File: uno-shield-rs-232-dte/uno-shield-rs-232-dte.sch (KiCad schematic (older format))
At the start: 19 parts, among them J1 Ctrl Route, J3 DSR/CTS, J4 DB9_Male, P1 Power, P2 Analog, P3 Digital, P4 Digital, P5 CONN_01X01, P7 CONN_01X01, U1 MAX232

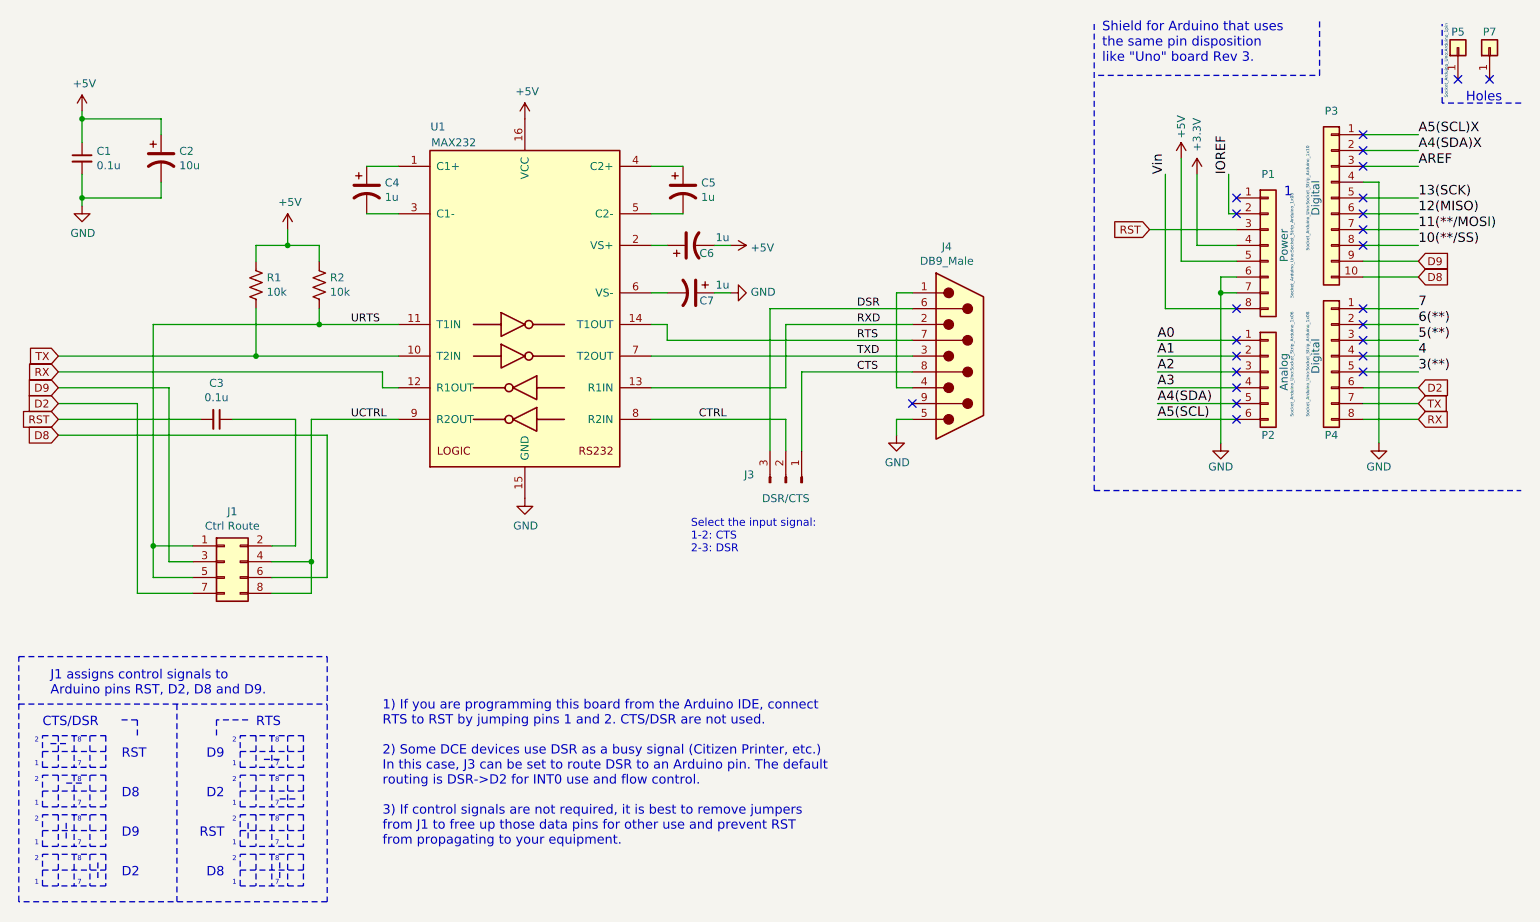
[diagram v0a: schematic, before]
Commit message: Adjust DTE shield to allow UART routing.
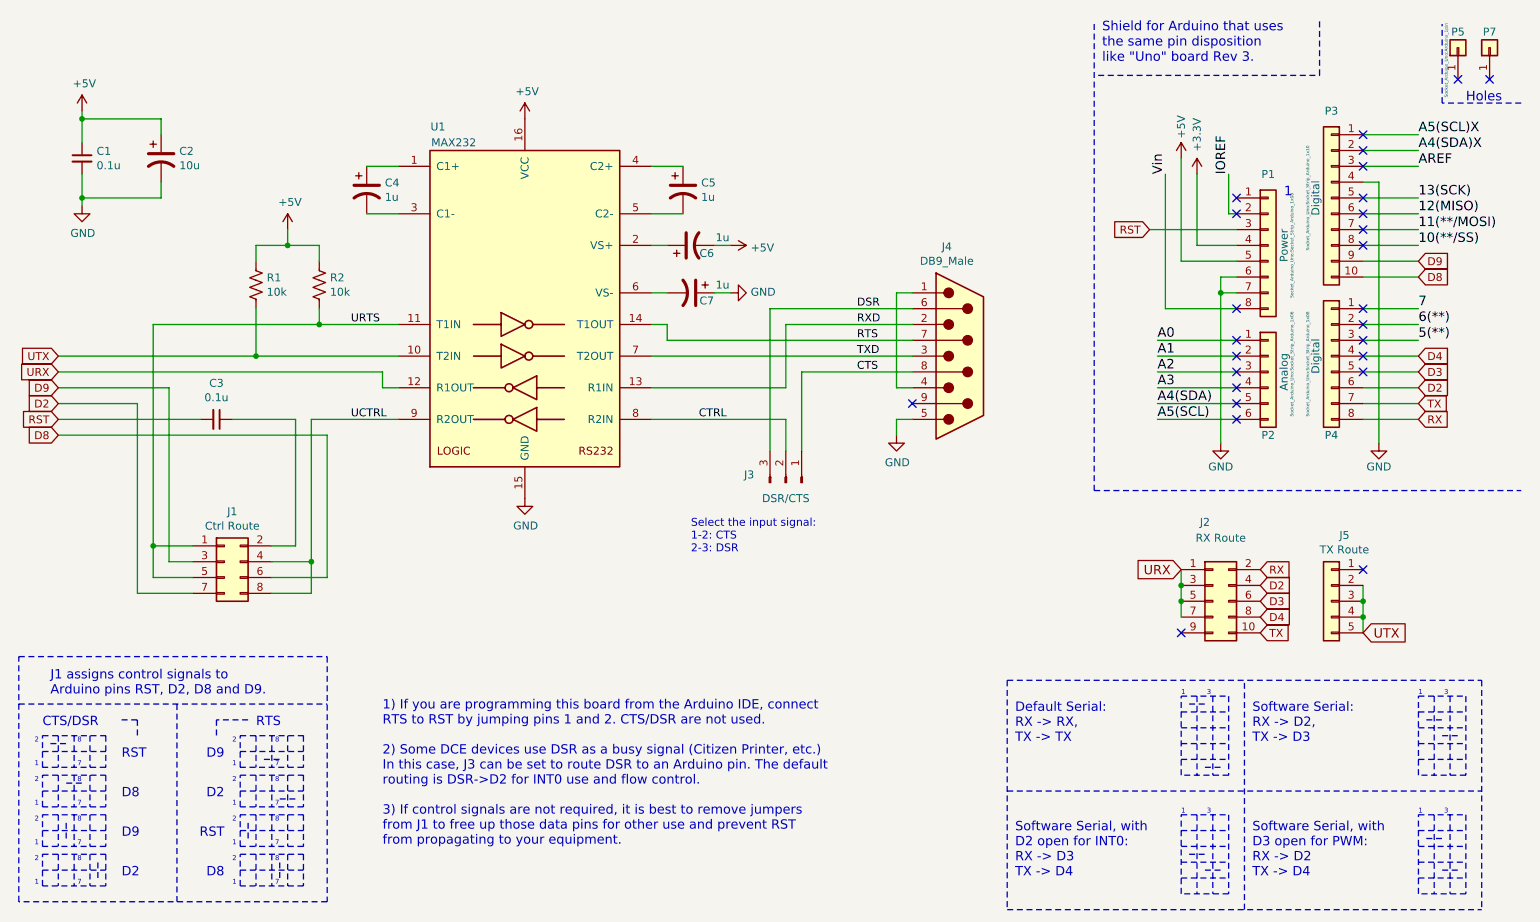
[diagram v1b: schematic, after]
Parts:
- added J2: RX Route, Connector_PinHeader_2.54mm:PinHeader_2x05_P2.54mm_Vertical, symbol Connector_Generic:Conn_02x05_Odd_Even
- added J5: TX Route, Connector_PinHeader_2.54mm:PinHeader_1x05_P2.54mm_Vertical, symbol Connector_Generic:Conn_01x05
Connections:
- net D2: now also J2.4 (Pin_4)
- net RX: now also J2.2 (Pin_2); no longer U1.12 (R1OUT)
- net TX: now also J2.10 (Pin_10); no longer R1.2, U1.10 (T2IN)
- net 3(**) renamed D3
- net D3: now also J2.6 (Pin_6)
- net 4 renamed D4
- net D4: now also J2.8 (Pin_8)
- new net URX: J2.1 (Pin_1), J2.3 (Pin_3), J2.5 (Pin_5), J2.7 (Pin_7), U1.12 (R1OUT)
- new net UTX: J5.2 (Pin_2), J5.3 (Pin_3), J5.4 (Pin_4), J5.5 (Pin_5), R1.2, U1.10 (T2IN)
- no-connect marks 24 -> 26
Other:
- note added: "1 3"
- note added: "Default Serial:\nRX -> RX,\nTX -> TX"
- note added: "Software Serial, with\nD2 open for INT0:\nRX -> D3\nTX -> D4"
- note added: "Software Serial, with\nD3 open for PWM:\nRX -> D2\nTX -> D4"
- note added: "Software Serial:\nRX -> D2,\nTX -> D3"
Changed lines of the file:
@@
 Text Label 8150 3100 0    60   ~ 0
 A5(SCL)
-Text Label 9800 2800 0    60   ~ 0
-3(**)
-Text Label 9800 2700 0    60   ~ 0
-4
 Text Label 9800 2600 0    60   ~ 0
 5(**)
@@
 Connection ~ 1350 1700
 Text GLabel 1200 2700 0    50   Input ~ 0
-TX
+UTX
 Text GLabel 1200 2800 0    50   Input ~ 0
-RX
+URX
 Text GLabel 1200 2900 0    50   Input ~ 0
 D9
@@
 Text Notes 3250 5800 0    59   ~ 0
 1) If you are programming this board from the Arduino IDE, connect\nRTS to RST by jumping pins 1 and 2. CTS/DSR are not used.\n\n2) Some DCE devices use DSR as a busy signal (Citizen Printer, etc.)\nIn this case, J3 can be set to route DSR to an Arduino pin. The default\nrouting is DSR->D2 for INT0 use and flow control.\n\n3) If control signals are not required, it is best to remove jumpers\nfrom J1 to free up those data pins for other use and prevent RST\nfrom propagating to your equipment.
+Text GLabel 8800 4050 2    50   Input ~ 0
+RX
+Text GLabel 8800 4150 2    50   Input ~ 0
+D2
+Text GLabel 8800 4250 2    50   Input ~ 0
+D3
+Text GLabel 8800 4350 2    50   Input ~ 0
+D4
+Text GLabel 8300 4050 0    59   Input ~ 0
+URX
+Connection ~ 8300 4150
+Wire Wire Line
+	8300 4150 8300 4050
+Connection ~ 8300 4250
+Wire Wire Line
+	8300 4150 8300 4250
+Wire Wire Line
+	8300 4350 8300 4250
+$Comp
+L Connector_Generic:Conn_02x05_Odd_Even J2
+U 1 1 603B3853
+P 8500 4250
+F 0 "J2" H 8450 4750 50  0000 C CNN
+F 1 "RX Route" H 8550 4650 50  0000 C CNN
+F 2 "Connector_PinHeader_2.54mm:PinHeader_2x05_P2.54mm_Vertical" H 8500 4250 50  0001 C CNN
+F 3 "~" H 8500 4250 50  0001 C CNN
+	1    8500 4250
+	1    0    0    -1
+$EndComp
+Text GLabel 8800 4450 2    50   Input ~ 0
+TX
+$Comp
+L Connector_Generic:Conn_01x05 J5
+U 1 1 603DA995
+P 9250 4250
+F 0 "J5" H 9168 4667 50  0000 C CNN
+F 1 "TX Route" H 9168 4576 50  0000 C CNN
+F 2 "Connector_PinHeader_2.54mm:PinHeader_1x05_P2.54mm_Vertical" H 9250 4250 50  0001 C CNN
+F 3 "~" H 9250 4250 50  0001 C CNN
+	1    9250 4250
+	-1   0    0    -1
+$EndComp
+Wire Wire Line
+	9450 4150 9450 4250
+Wire Wire Line
+	9450 4250 9450 4350
+Connection ~ 9450 4250
+Wire Wire Line
+	9450 4350 9450 4450
+Connection ~ 9450 4350
+Text GLabel 9450 4450 2    59   Input ~ 0
+UTX
+NoConn ~ 9450 4050
+NoConn ~ 8300 4450
+Wire Notes Line
+	8300 4850 8600 4850
+Wire Notes Line
+	8600 4850 8600 5350
+Wire Notes Line
+	8600 5350 8300 5350
+Wire Notes Line
+	8300 5350 8300 4850
+Wire Notes Line
+	8300 4950 8600 4950
+Wire Notes Line
+	8300 5050 8600 5050
+Wire Notes Line
+	8300 5150 8600 5150
+Wire Notes Line
+	8300 5250 8600 5250
+Wire Notes Line
+	8400 4850 8400 5350
+Wire Notes Line
+	8500 4850 8500 5350
+Text Notes 8300 4850 0    31   ~ 0
+1          3
+Wire Notes Line
+	8300 5600 8600 5600
+Wire Notes Line
+	8600 5600 8600 6100
+Wire Notes Line
+	8600 6100 8300 6100
+Wire Notes Line
+	8300 6100 8300 5600
+Wire Notes Line
+	8300 5700 8600 5700
+Wire Notes Line
+	8300 5800 8600 5800
+Wire Notes Line
+	8300 5900 8600 5900
+Wire Notes Line
+	8300 6000 8600 6000
+Wire Notes Line
+	8400 5600 8400 6100
+Wire Notes Line
+	8500 5600 8500 6100
+Text Notes 8300 5600 0    31   ~ 0
+1          3
+Wire Notes Line
+	9800 4850 10100 4850
+Wire Notes Line
+	10100 4850 10100 5350
+Wire Notes Line
+	10100 5350 9800 5350
+Wire Notes Line
+	9800 5350 9800 4850
+Wire Notes Line
+	9800 4950 10100 4950
+Wire Notes Line
+	9800 5050 10100 5050
+Wire Notes Line
+	9800 5150 10100 5150
+Wire Notes Line
+	9800 5250 10100 5250
+Wire Notes Line
+	9900 4850 9900 5350
+Wire Notes Line
+	10000 4850 10000 5350
+Text Notes 9800 4850 0    31   ~ 0
+1          3
+Wire Notes Line
+	9800 5600 10100 5600
+Wire Notes Line
+	10100 5600 10100 6100
+Wire Notes Line
+	10100 6100 9800 6100
+Wire Notes Line
+	9800 6100 9800 5600
+Wire Notes Line
+	9800 5700 10100 5700
+Wire Notes Line
+	9800 5800 10100 5800
+Wire Notes Line
+	9800 5900 10100 5900
+Wire Notes Line
+	9800 6000 10100 6000
+Wire Notes Line
+	9900 5600 9900 6100
+Wire Notes Line
+	10000 5600 10000 6100
+Text Notes 9800 5600 0    31   ~ 0
+1          3
+Wire Notes Line width 100
+	8350 4900 8450 4900
+Wire Notes Line width 100
+	8450 5300 8550 5300
+Wire Notes Line width 100
+	9850 5000 9950 5000
+Wire Notes Line width 100
+	9950 5100 10050 5100
+Wire Notes Line width 100
+	9850 5750 9950 5750
+Wire Notes Line width 100
+	9950 5950 10050 5950
+Wire Notes Line width 100
+	8350 5850 8450 5850
+Wire Notes Line width 100
+	8450 5950 8550 5950
+Text Notes 7250 5150 0    59   ~ 0
+Default Serial:\nRX -> RX,\nTX -> TX
+Text Notes 8750 5150 0    59   ~ 0
+Software Serial:\nRX -> D2,\nTX -> D3
+Text Notes 8750 6000 0    59   ~ 0
+Software Serial, with\nD3 open for PWM:\nRX -> D2\nTX -> D4
+Text Notes 7250 6000 0    59   ~ 0
+Software Serial, with\nD2 open for INT0:\nRX -> D3\nTX -> D4
+Wire Notes Line
+	8700 6200 8700 4750
+Wire Notes Line
+	7200 4750 7200 6200
+Wire Notes Line
+	7200 6200 10200 6200
+Wire Notes Line
+	7200 4750 10200 4750
+Wire Notes Line
+	7200 5450 10200 5450
+Wire Notes Line
+	10200 4750 10200 6200
+Text GLabel 9800 2800 2    50   Input ~ 0
+D3
+Text GLabel 9800 2700 2    50   Input ~ 0
+D4
 $EndSCHEMATC
